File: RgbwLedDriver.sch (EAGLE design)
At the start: 47 parts, among them CN1 LED1, CN2 LED2, CN3 LED3, CN4 LED4, CN5 POWER, CN6 I2C, CN7 POWER, CN8 I2C, IC1 PCA9685BS, J1 A0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

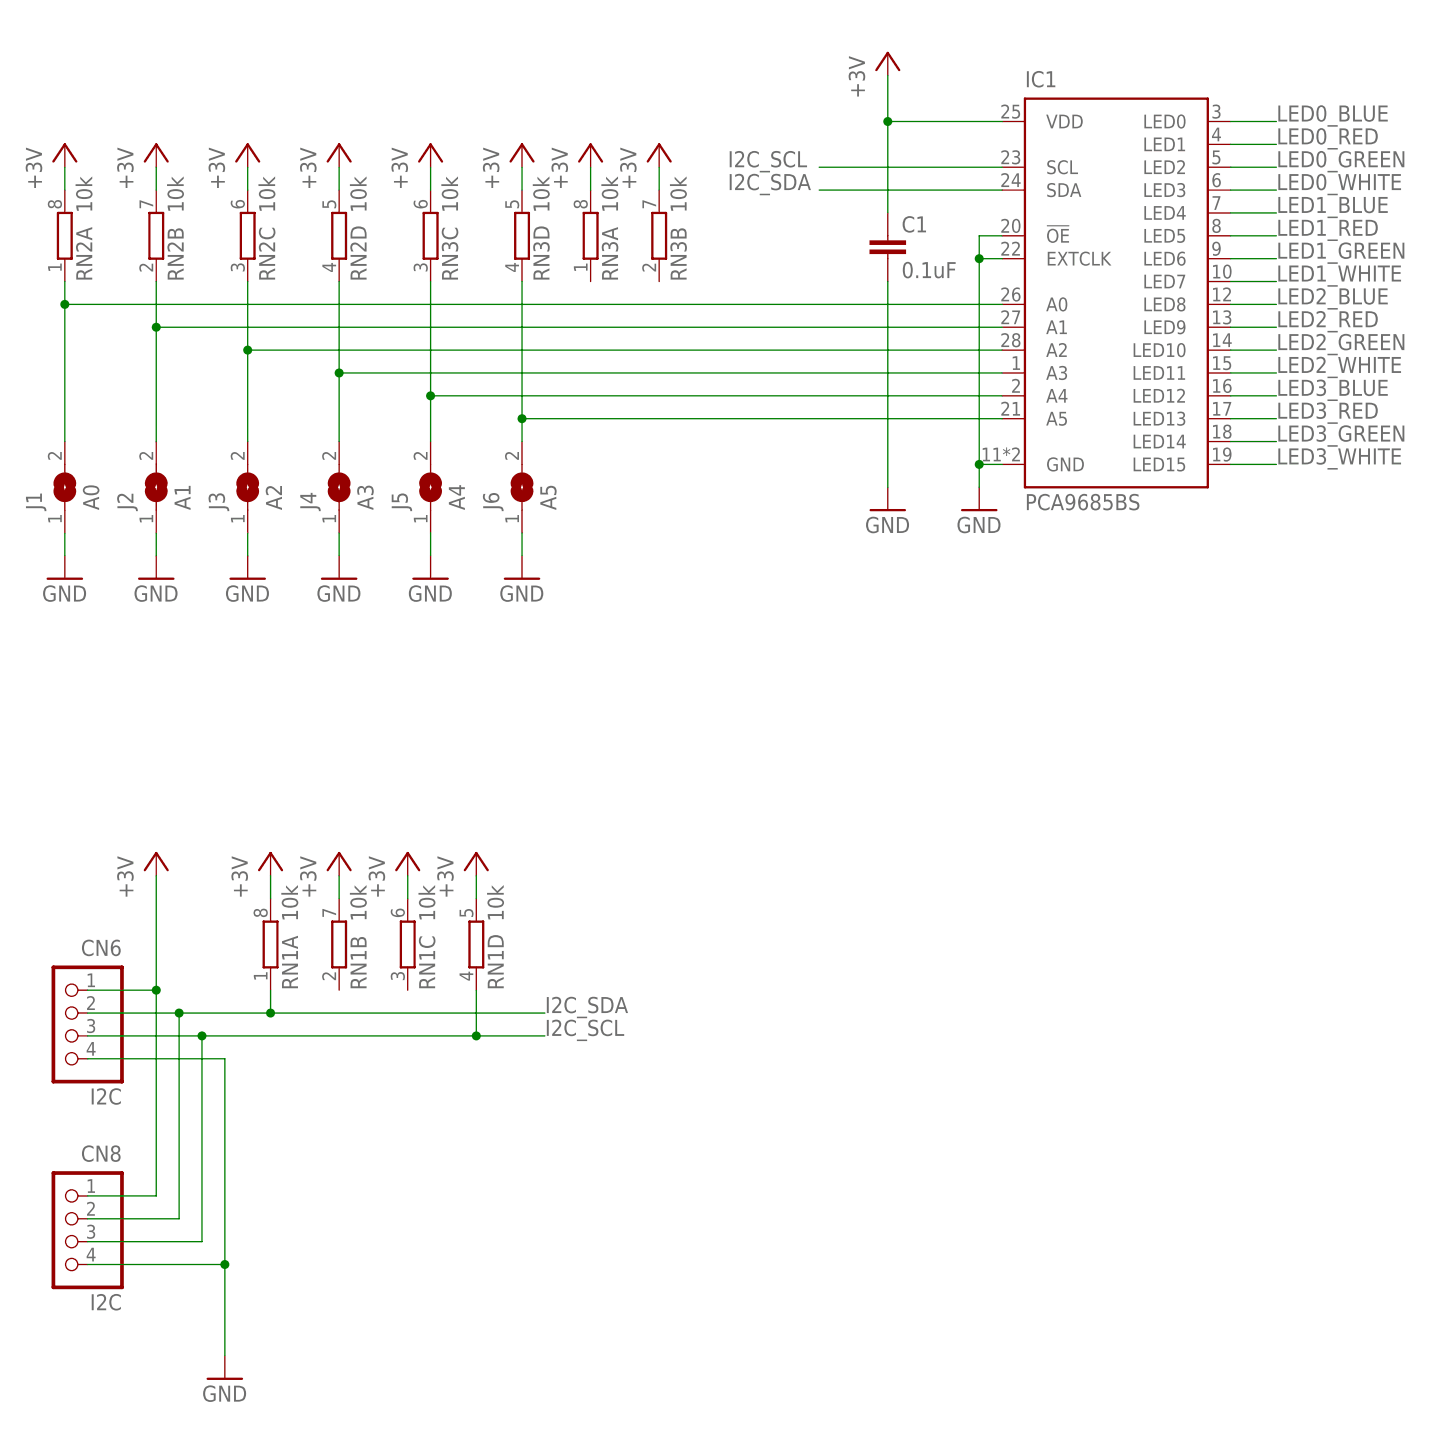
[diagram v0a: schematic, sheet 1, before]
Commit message: 電源のシンボルを変更
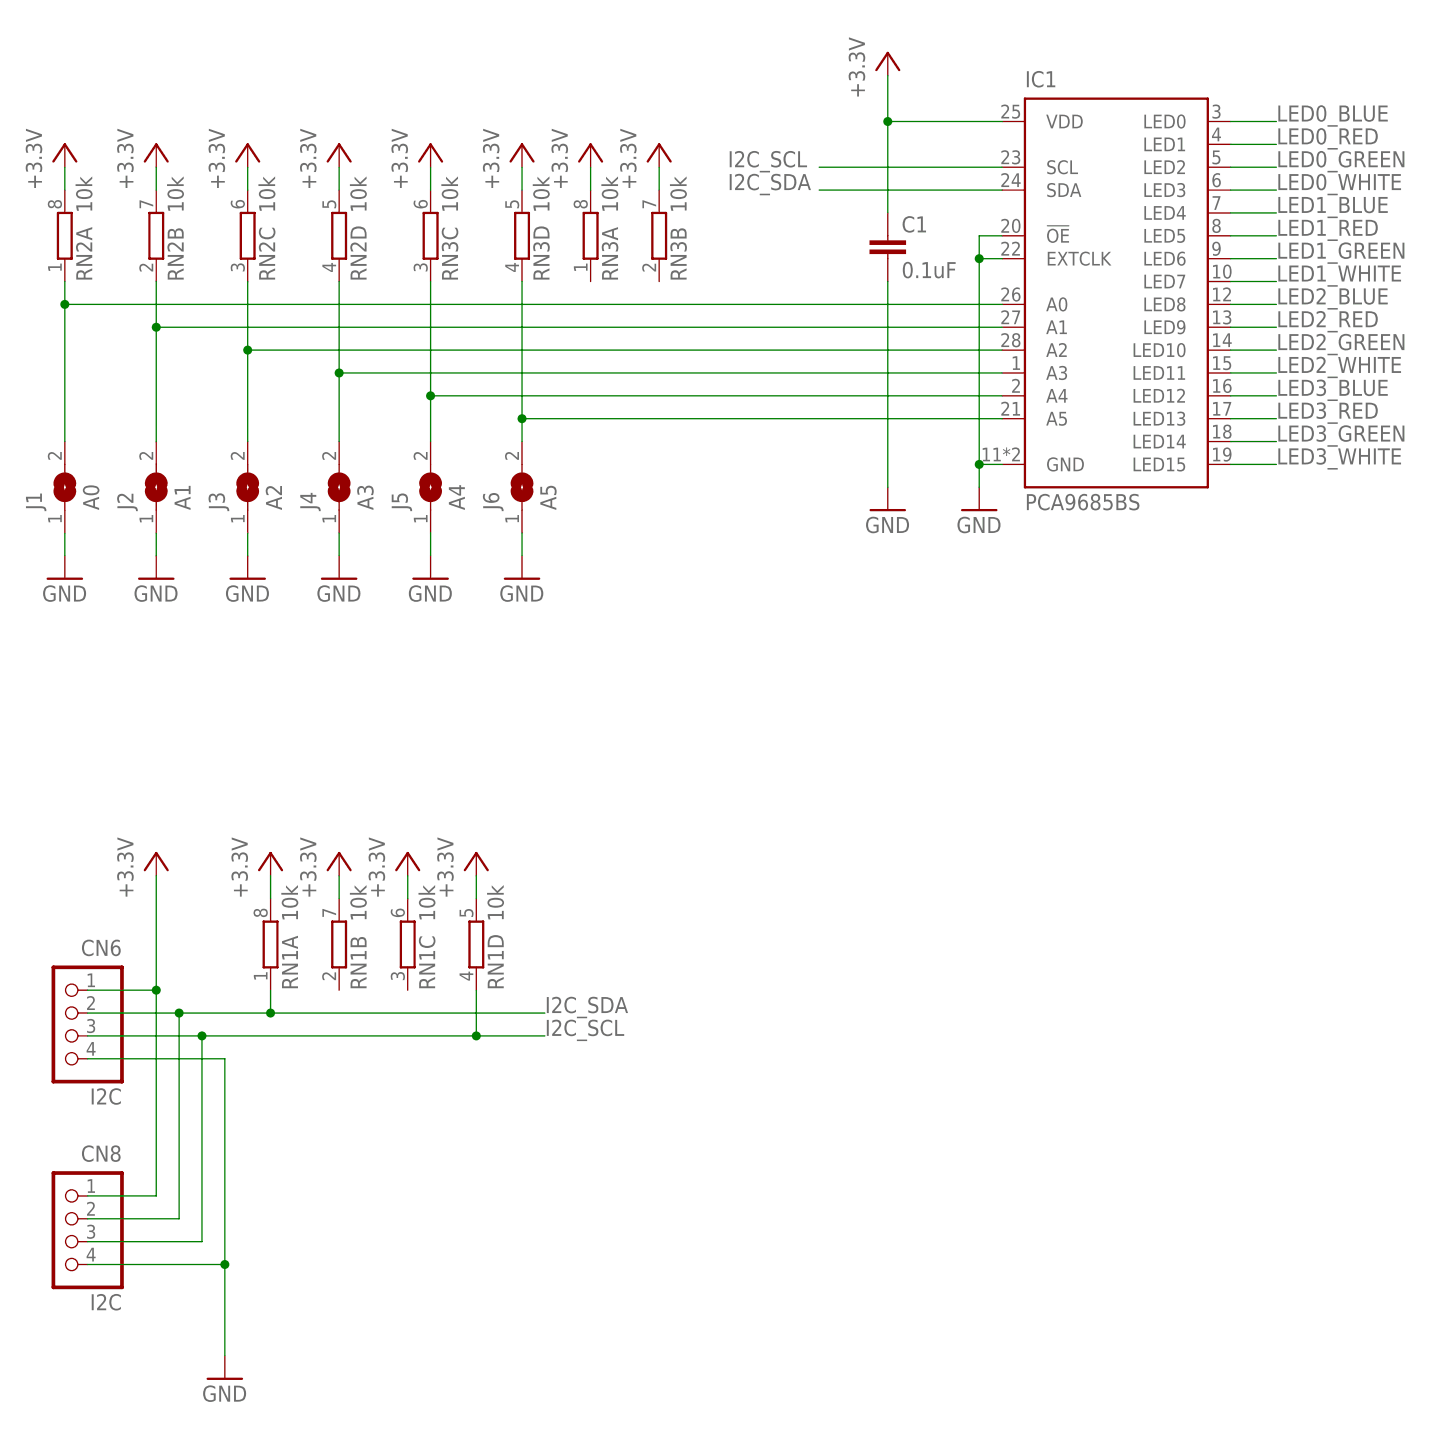
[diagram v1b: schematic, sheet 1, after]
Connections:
- net +3V renamed +3.3V
- net +7.2V renamed +7.4V
